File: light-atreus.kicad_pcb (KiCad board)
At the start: 2 copper layers, 40.1 x 37.5 mm, 10 parts, among them J1 USB_B, J11 USB_B, J2 CONN_01X02, J3 CONN_01X02, J4 CONN_01X02, J5 CONN_01X02, J6 CONN_01X02, J7 CONN_01X02, J8 CONN_01X02, J9 CONN_01X02

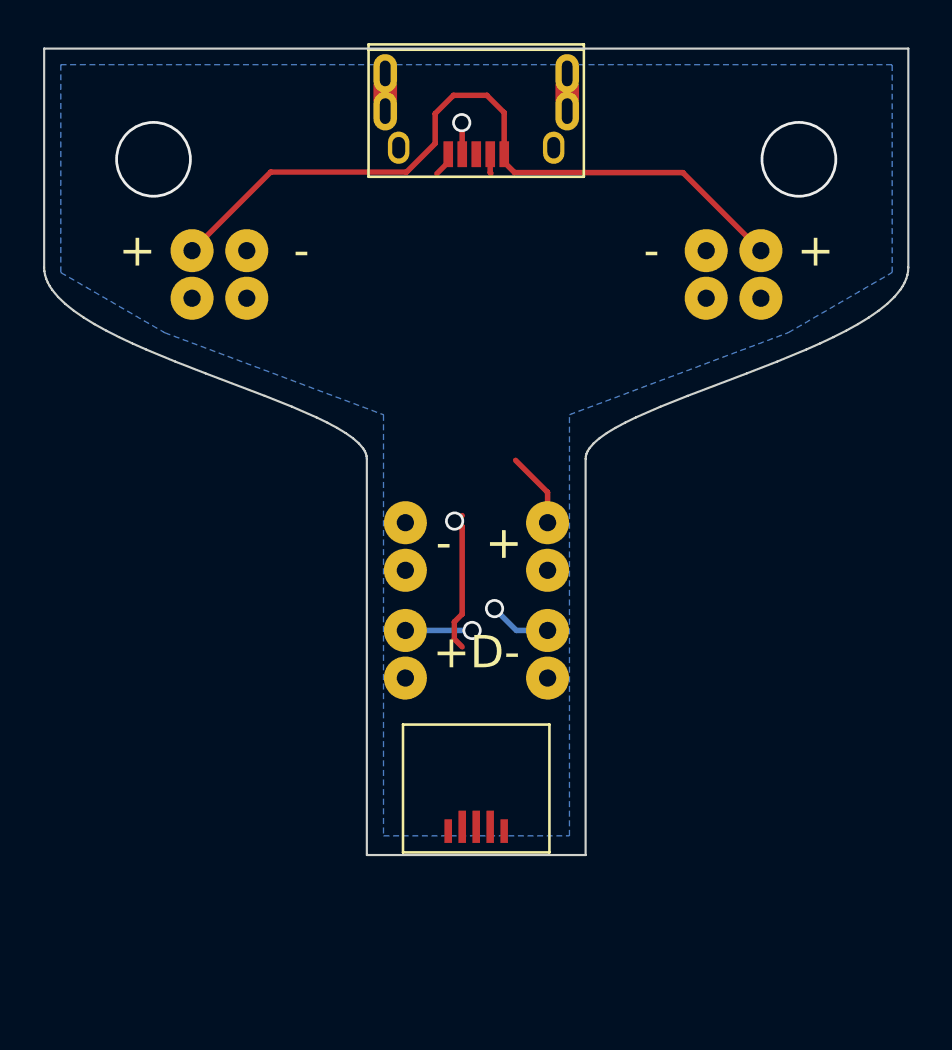
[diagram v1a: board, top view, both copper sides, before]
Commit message: Reroute traces at new length
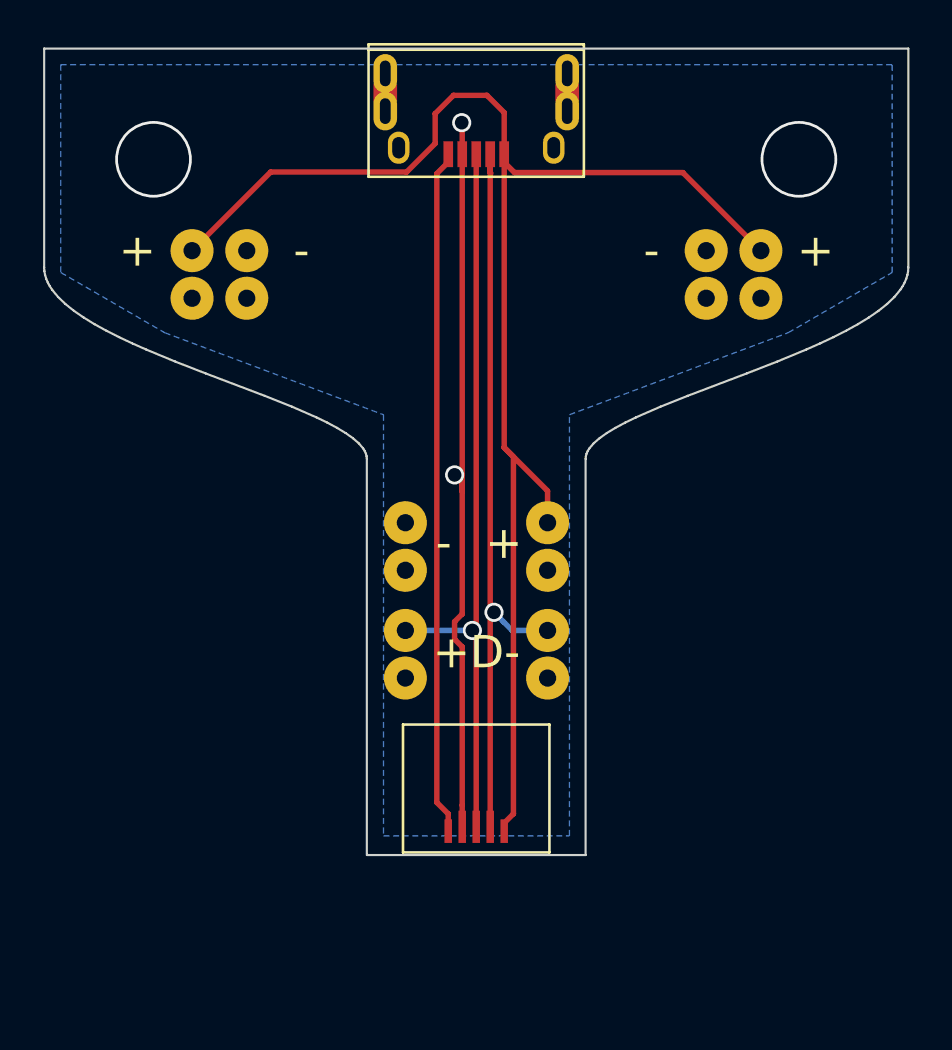
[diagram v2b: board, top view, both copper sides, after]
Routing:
- net /VBUS: track 38.1 -> 70.7 mm
- net /D+: track 3.28 -> 34.7 mm
- net /D-: track 3.79 -> 35.1 mm
- net /SHIELD: track 1.12 -> 31.9 mm
- net /GND: track 8.28 -> 33.9 mm
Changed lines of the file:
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@@
     (thickness 1.6)
     (drawings 73)
-    (tracks 38)
+    (tracks 56)
     (zones 0)
     (modules 10)
@@
   (via (at 145.2753 76.0222) (size 3.556) (drill 3.302) (layers F.Cu B.Cu) (net 0) (status 40000))
   (via (at 115.3033 76.0222) (size 3.556) (drill 3.302) (layers F.Cu B.Cu) (net 0) (status 40000))
-  (segment (start 128.9893 76.159) (end 128.9893 75.784) (width 0.254) (layer F.Cu) (net 1))
-  (segment (start 128.460498 76.687802) (end 128.9893 76.159) (width 0.254) (layer F.Cu) (net 1))
-  (segment (start 129.286 92.822) (end 129.3853 92.822) (width 0.254) (layer F.Cu) (net 2))
-  (segment (start 129.3853 92.822) (end 129.6393 92.568) (width 0.254) (layer F.Cu) (net 2))
-  (segment (start 129.6393 93.076) (end 129.6393 97.139758) (width 0.254) (layer F.Cu) (net 2))
-  (segment (start 129.6393 93.076) (end 129.54 93.076) (width 0.254) (layer F.Cu) (net 2))
-  (segment (start 129.54 93.076) (end 129.286 92.822) (width 0.254) (layer F.Cu) (net 2))
-  (via (at 129.286 92.822) (size 0.889) (drill 0.635) (layers F.Cu B.Cu) (net 2))
-  (segment (start 129.273299 98.298241) (end 129.6393 98.664242) (width 0.254) (layer F.Cu) (net 2))
-  (segment (start 129.273299 97.505759) (end 129.273299 98.298241) (width 0.254) (layer F.Cu) (net 2))
-  (segment (start 129.6393 97.139758) (end 129.273299 97.505759) (width 0.254) (layer F.Cu) (net 2))
+  (segment (start 128.9893 106.4166) (end 128.9893 107.2206) (width 0.254) (layer F.Cu) (net 1))
+  (segment (start 128.460498 105.887798) (end 128.9893 106.4166) (width 0.254) (layer F.Cu) (net 1))
+  (segment (start 128.9893 75.784) (end 128.9893 76.159) (width 0.254) (layer F.Cu) (net 1))
+  (segment (start 128.460498 76.687802) (end 128.460498 105.887798) (width 0.254) (layer F.Cu) (net 1))
+  (segment (start 128.9893 76.159) (end 128.460498 76.687802) (width 0.254) (layer F.Cu) (net 1))
+  (segment (start 129.6393 91.0313) (end 129.286 90.678) (width 0.254) (layer F.Cu) (net 2))
+  (segment (start 129.6393 91.44) (end 129.6393 97.139758) (width 0.254) (layer F.Cu) (net 2))
+  (segment (start 129.6393 75.784) (end 129.6393 91.44) (width 0.254) (layer F.Cu) (net 2))
+  (segment (start 129.6393 91.44) (end 129.6393 91.0313) (width 0.254) (layer F.Cu) (net 2))
+  (via (at 129.286 90.678) (size 0.889) (drill 0.635) (layers F.Cu B.Cu) (net 2))
+  (segment (start 129.6393 106.0166) (end 129.6393 107.0206) (width 0.254) (layer F.Cu) (net 2))
+  (segment (start 129.6393 98.664242) (end 129.6393 106.0166) (width 0.254) (layer F.Cu) (net 2))
+  (segment (start 129.286011 98.310953) (end 129.6393 98.664242) (width 0.254) (layer F.Cu) (net 2))
+  (segment (start 129.286011 97.493047) (end 129.286011 98.310953) (width 0.254) (layer F.Cu) (net 2))
+  (segment (start 129.6393 97.139758) (end 129.286011 97.493047) (width 0.254) (layer F.Cu) (net 2))
   (segment (start 129.6393 75.784) (end 129.6393 74.3435) (width 0.254) (layer F.Cu) (net 2))
   (segment (start 129.6393 74.3435) (end 129.6162 74.3204) (width 0.254) (layer F.Cu) (net 2))
   (via (at 129.6162 74.3204) (size 0.889) (drill 0.635) (layers F.Cu B.Cu) (net 2))
-  (segment (start 127 97.902) (end 130.0988 97.902) (width 0.254) (layer B.Cu) (net 3))
-  (segment (start 130.2766 97.902) (end 130.0988 97.902) (width 0.254) (layer B.Cu) (net 3))
-  (via (at 130.0988 97.902) (size 0.889) (drill 0.635) (layers F.Cu B.Cu) (net 3))
-  (segment (start 133.604 97.902) (end 132.1562 97.902) (width 0.254) (layer B.Cu) (net 4))
-  (segment (start 132.1562 97.902) (end 131.1402 96.886) (width 0.254) (layer B.Cu) (net 4))
-  (via (at 131.1402 96.886) (size 0.889) (drill 0.635) (layers F.Cu B.Cu) (net 4))
+  (segment (start 130.2893 107.0206) (end 130.2893 98.079779) (width 0.254) (layer F.Cu) (net 3))
+  (segment (start 130.2893 75.784) (end 130.2893 97.724221) (width 0.254) (layer F.Cu) (net 3))
+  (segment (start 130.2893 98.079779) (end 130.111521 97.902) (width 0.254) (layer F.Cu) (net 3))
+  (via (at 130.111521 97.902) (size 0.889) (drill 0.635) (layers F.Cu B.Cu) (net 3))
+  (segment (start 130.2766 97.902) (end 130.111521 97.902) (width 0.254) (layer B.Cu) (net 3))
+  (segment (start 127 97.902) (end 130.111521 97.902) (width 0.254) (layer B.Cu) (net 3))
+  (segment (start 130.2893 97.724221) (end 130.111521 97.902) (width 0.254) (layer F.Cu) (net 3))
+  (segment (start 131.559309 97.504025) (end 131.11481 97.059526) (width 0.254) (layer B.Cu) (net 4))
+  (segment (start 131.957284 97.902) (end 131.559309 97.504025) (width 0.254) (layer B.Cu) (net 4))
+  (segment (start 133.604 97.902) (end 131.957284 97.902) (width 0.254) (layer B.Cu) (net 4))
+  (segment (start 130.9393 107.0206) (end 130.9393 97.235036) (width 0.254) (layer F.Cu) (net 4))
+  (segment (start 130.9393 96.884016) (end 131.11481 97.059526) (width 0.254) (layer F.Cu) (net 4))
+  (segment (start 130.9393 97.235036) (end 131.11481 97.059526) (width 0.254) (layer F.Cu) (net 4))
+  (via (at 131.11481 97.059526) (size 0.889) (drill 0.635) (layers F.Cu B.Cu) (net 4))
+  (segment (start 130.9393 75.784) (end 130.9393 96.884016) (width 0.254) (layer F.Cu) (net 4))
   (segment (start 130.9393 76.638) (end 130.975101 76.673801) (width 0.254) (layer F.Cu) (net 4))
   (segment (start 130.9393 75.784) (end 130.9393 76.638) (width 0.254) (layer F.Cu) (net 4))
+  (segment (start 131.5893 106.8456) (end 131.5893 107.2206) (width 0.254) (layer F.Cu) (net 5))
+  (segment (start 132.0183 106.4166) (end 131.5893 106.8456) (width 0.254) (layer F.Cu) (net 5))
+  (segment (start 132.0183 89.837) (end 132.0183 106.4166) (width 0.254) (layer F.Cu) (net 5))
+  (segment (start 131.5893 89.408) (end 132.0183 89.837) (width 0.254) (layer F.Cu) (net 5))
+  (segment (start 131.5893 75.784) (end 131.5893 89.408) (width 0.254) (layer F.Cu) (net 5))
+  (segment (start 133.604 92.898) (end 133.604 91.4227) (width 0.254) (layer F.Cu) (net 5))
+  (segment (start 133.604 91.4227) (end 131.5893 89.408) (width 0.254) (layer F.Cu) (net 5))
   (segment (start 117.094 80.264) (end 120.74299 76.61501) (width 0.254) (layer F.Cu) (net 5))
   (segment (start 120.74299 76.61501) (end 127.054226 76.61501) (width 0.254) (layer F.Cu) (net 5))
@@
   (segment (start 143.51 80.264) (end 139.884 76.638) (width 0.254) (layer F.Cu) (net 5))
   (segment (start 139.884 76.638) (end 132.0683 76.638) (width 0.254) (layer F.Cu) (net 5))
-  (segment (start 133.604 92.898) (end 133.604 91.484508) (width 0.254) (layer F.Cu) (net 5))
-  (segment (start 133.604 91.484508) (end 132.122092 90.0026) (width 0.254) (layer F.Cu) (net 5))
   (segment (start 131.5893 76.159) (end 132.0683 76.638) (width 0.254) (layer F.Cu) (net 5))
   (segment (start 131.5893 75.784) (end 131.5893 76.159) (width 0.254) (layer F.Cu) (net 5))

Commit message: Move LED power breakouts out of the way of the case!
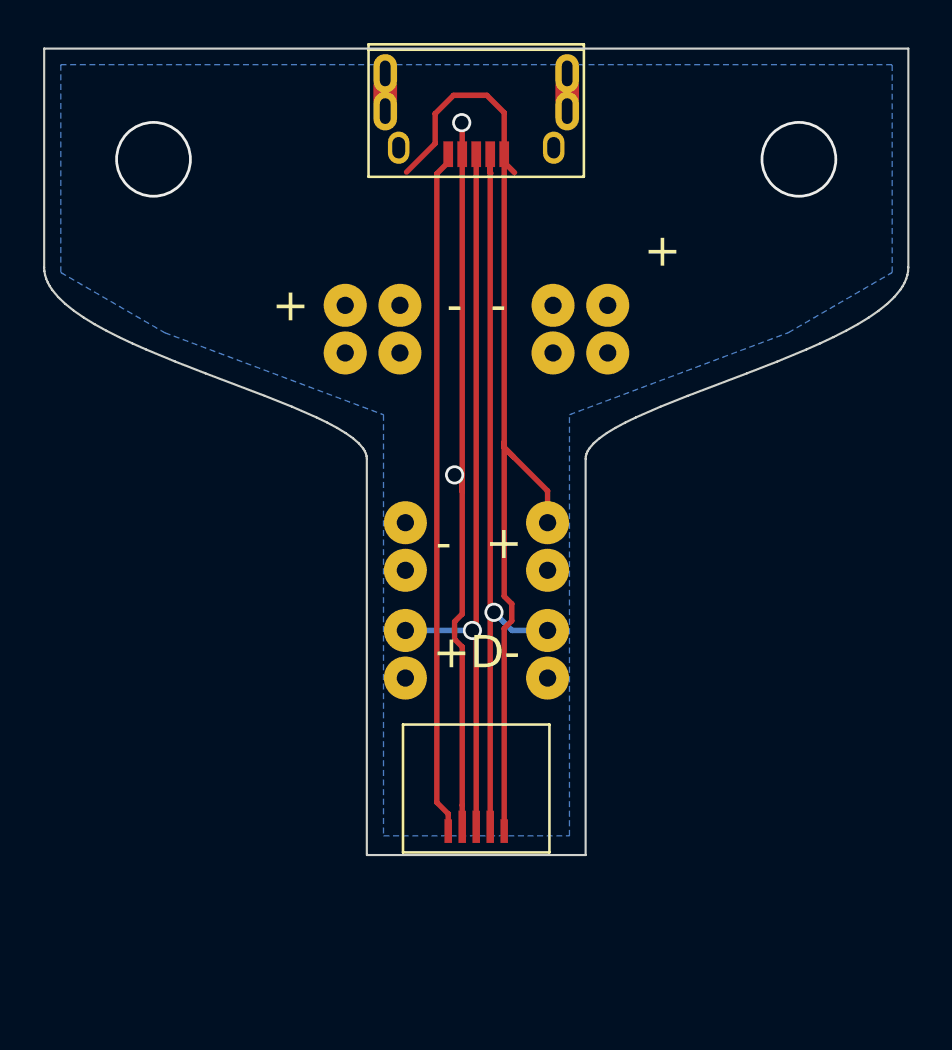
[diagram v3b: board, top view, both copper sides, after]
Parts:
- moved J4 7.55 mm to (124.2, 83.9)
- moved J2 7.55 mm to (136.4, 83.9)
- moved J3 7.55 mm to (133.9, 83.9)
- moved J5 7.55 mm to (126.7, 83.9)
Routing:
- net /VBUS: track 70.7 -> 47.4 mm
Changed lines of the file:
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@@
   (general
     (thickness 1.6)
-    (drawings 73)
+    (drawings 74)
     (tracks 56)
     (zones 0)
@@
   )
   (module custom_footprints:SolderWirePad_1x2-8mm (layer F.Cu)
-    (at 143.51 81.374 270)
+    (at 136.398 83.914 270)
     (fp_text reference J2 (at 0 -3.81 270) (layer Cmts.User)
       (effects (font (size 1 1) (thickness 0.15)))
@@
   )
   (module custom_footprints:SolderWirePad_1x2-8mm (layer F.Cu)
-    (at 140.97 81.374 270)
+    (at 133.858 83.914 270)
     (fp_text reference J3 (at 0 -3.81 270) (layer Cmts.User)
       (effects (font (size 1 1) (thickness 0.15)))
@@
   )
   (module custom_footprints:SolderWirePad_1x2-8mm (layer F.Cu)
-    (at 117.094 81.374 270)
+    (at 124.206 83.914 270)
     (fp_text reference J4 (at 0 -3.81 270) (layer Cmts.User) hide
       (effects (font (size 1 1) (thickness 0.15)))
@@
   )
   (module custom_footprints:SolderWirePad_1x2-8mm (layer F.Cu)
-    (at 119.634 81.374 270)
+    (at 126.746 83.914 270)
     (fp_text reference J5 (at 0 -3.81 270) (layer Cmts.User)
       (effects (font (size 1 1) (thickness 0.15)))
@@
       (net 5 /VBUS))
   )
+  (gr_line (start 147.574 83.566) (end 113.03 83.566) (layer Cmts.User) (width 0.2))
   (gr_text - (at 128.778 93.838) (layer F.SilkS)
     (effects (font (size 1.5 1.5) (thickness 0.3)))
@@
     (effects (font (size 1.5 1.5) (thickness 0.3)))
   )
-  (gr_text + (at 146.05 80.264) (layer F.SilkS)
-    (effects (font (size 1.5 1.5) (thickness 0.3)))
-  )
-  (gr_text - (at 138.43 80.264) (layer F.SilkS)
-    (effects (font (size 1.5 1.5) (thickness 0.3)))
-  )
-  (gr_text - (at 122.174 80.264) (layer F.SilkS)
-    (effects (font (size 1.5 1.5) (thickness 0.3)))
-  )
-  (gr_text + (at 114.554 80.264) (layer F.SilkS)
+  (gr_text + (at 138.938 80.264) (layer F.SilkS)
+    (effects (font (size 1.5 1.5) (thickness 0.3)))
+  )
+  (gr_text - (at 131.318 82.804) (layer F.SilkS)
+    (effects (font (size 1.5 1.5) (thickness 0.3)))
+  )
+  (gr_text - (at 129.286 82.804) (layer F.SilkS)
+    (effects (font (size 1.5 1.5) (thickness 0.3)))
+  )
+  (gr_text + (at 121.666 82.804) (layer F.SilkS)
     (effects (font (size 1.5 1.5) (thickness 0.3)))
   )
@@
   (segment (start 130.9393 76.638) (end 130.975101 76.673801) (width 0.254) (layer F.Cu) (net 4))
   (segment (start 130.9393 75.784) (end 130.9393 76.638) (width 0.254) (layer F.Cu) (net 4))
+  (segment (start 131.5893 75.784) (end 131.5893 89.154) (width 0.254) (layer F.Cu) (net 5))
+  (segment (start 131.5893 89.154) (end 131.5893 89.408) (width 0.254) (layer F.Cu) (net 5))
+  (segment (start 131.5893 107.2206) (end 131.5893 97.806778) (width 0.254) (layer F.Cu) (net 5))
+  (segment (start 131.5893 97.806778) (end 131.940311 97.455767) (width 0.254) (layer F.Cu) (net 5))
+  (segment (start 131.940311 97.455767) (end 131.940311 96.663285) (width 0.254) (layer F.Cu) (net 5))
+  (segment (start 131.940311 96.663285) (end 131.5893 96.312274) (width 0.254) (layer F.Cu) (net 5))
+  (segment (start 131.5893 96.312274) (end 131.5893 89.154) (width 0.254) (layer F.Cu) (net 5))
   (segment (start 131.5893 106.8456) (end 131.5893 107.2206) (width 0.254) (layer F.Cu) (net 5))
-  (segment (start 132.0183 106.4166) (end 131.5893 106.8456) (width 0.254) (layer F.Cu) (net 5))
-  (segment (start 132.0183 89.837) (end 132.0183 106.4166) (width 0.254) (layer F.Cu) (net 5))
   (segment (start 131.5893 89.408) (end 132.0183 89.837) (width 0.254) (layer F.Cu) (net 5))
-  (segment (start 131.5893 75.784) (end 131.5893 89.408) (width 0.254) (layer F.Cu) (net 5))
   (segment (start 133.604 92.898) (end 133.604 91.4227) (width 0.254) (layer F.Cu) (net 5))
   (segment (start 133.604 91.4227) (end 131.5893 89.408) (width 0.254) (layer F.Cu) (net 5))
-  (segment (start 117.094 80.264) (end 120.74299 76.61501) (width 0.254) (layer F.Cu) (net 5))
-  (segment (start 120.74299 76.61501) (end 127.054226 76.61501) (width 0.254) (layer F.Cu) (net 5))
   (segment (start 131.5893 73.8551) (end 131.5893 75.784) (width 0.254) (layer F.Cu) (net 5))
   (segment (start 127.054226 76.61501) (end 128.383299 75.285937) (width 0.254) (layer F.Cu) (net 5))
@@
   (segment (start 129.2352 73.0504) (end 130.7846 73.0504) (width 0.254) (layer F.Cu) (net 5))
   (segment (start 130.7846 73.0504) (end 131.5893 73.8551) (width 0.254) (layer F.Cu) (net 5))
-  (segment (start 143.51 80.264) (end 139.884 76.638) (width 0.254) (layer F.Cu) (net 5))
-  (segment (start 139.884 76.638) (end 132.0683 76.638) (width 0.254) (layer F.Cu) (net 5))
   (segment (start 131.5893 76.159) (end 132.0683 76.638) (width 0.254) (layer F.Cu) (net 5))
   (segment (start 131.5893 75.784) (end 131.5893 76.159) (width 0.254) (layer F.Cu) (net 5))
